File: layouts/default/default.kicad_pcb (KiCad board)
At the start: 2 copper layers, 27.1 x 34.7 mm, 18 parts

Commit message: fixed button
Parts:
- moved R3 0.10 mm to (77.1, 82.3)
- moved U3 0.07 mm to (73.2, 82.3)
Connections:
- net SUB2 renamed B8
- C1 pad 1: hv-1 -> hv
- C2 pad 1: hv -> hv-1
- C3 pad 1: hv -> hv-1
- C4 pad 1: hv -> hv-1
- C5 pad 1: hv -> hv-1
- C6 pad 1: hv -> hv-1
- C7 pad 1: hv -> hv-1
- R3 pad 1: hv -> hv-1
- U1 pad 2: hv -> hv-1
- U1 pad 3: hv-1 -> hv
- U1 pad 4: hv -> hv-1
- U2 pad 8: hv -> hv-1
- U4 pad 2: hv -> hv-1
- U5 pad A4: hv-1 -> hv
- U5 pad A9: hv-1 -> hv
- U5 pad B4: hv-1 -> hv
- U5 pad B9: hv-1 -> hv
- U6 pad 4: hv -> hv-1
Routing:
- net hv-1: track 27.3 -> 58.7 mm, vias 2 -> 4
- net hv: track 58.6 -> 27.3 mm, vias 4 -> 2

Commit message: updated button
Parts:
- removed R3: 10kΩ ±1% 62.5mW, atopile:R0402-56259e
- removed U3: , lib:KEY-SMD_4P-L4.2-W3.2-P2.20-LS4.6
- added R6: 10kΩ ±1% 62.5mW, atopile:R0402-56259e, F.Cu at (77.2, 82.2)
- added U7: , lib:KEY-SMD_4P-L4.2-W3.2-P2.20-LS4.6, F.Cu at (73.2, 82.2)
- C1, C2: value 10µF ±10% 25V X5R -> 100nF ±10% 50V X7R
- R1, R2: value 1kΩ ±1% 62.5mW -> 10kΩ ±1% 62.5mW
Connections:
- C1 pad 1: hv -> hv-1
- C2 pad 1: hv-1 -> hv
- C3 pad 1: hv-1 -> hv
- C4 pad 1: hv-1 -> hv
- C5 pad 1: hv-1 -> hv
- C6 pad 1: hv-1 -> hv
- C7 pad 1: hv-1 -> hv
- U1 pad 2: hv-1 -> hv
- U1 pad 3: hv -> hv-1
- U1 pad 4: hv-1 -> hv
- U2 pad 8: hv-1 -> hv
- U4 pad 2: hv-1 -> hv
- U4 pad 3: in -> EN
- U5 pad A4: hv -> hv-1
- U5 pad A9: hv -> hv-1
- U5 pad B4: hv -> hv-1
- U5 pad B9: hv -> hv-1
- U6 pad 4: hv-1 -> hv
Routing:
- net hv-1: track 58.7 -> 27.3 mm, vias 4 -> 2
- net hv: track 27.3 -> 58.7 mm, vias 2 -> 4
- net in: track 16.4 -> 18.7 mm

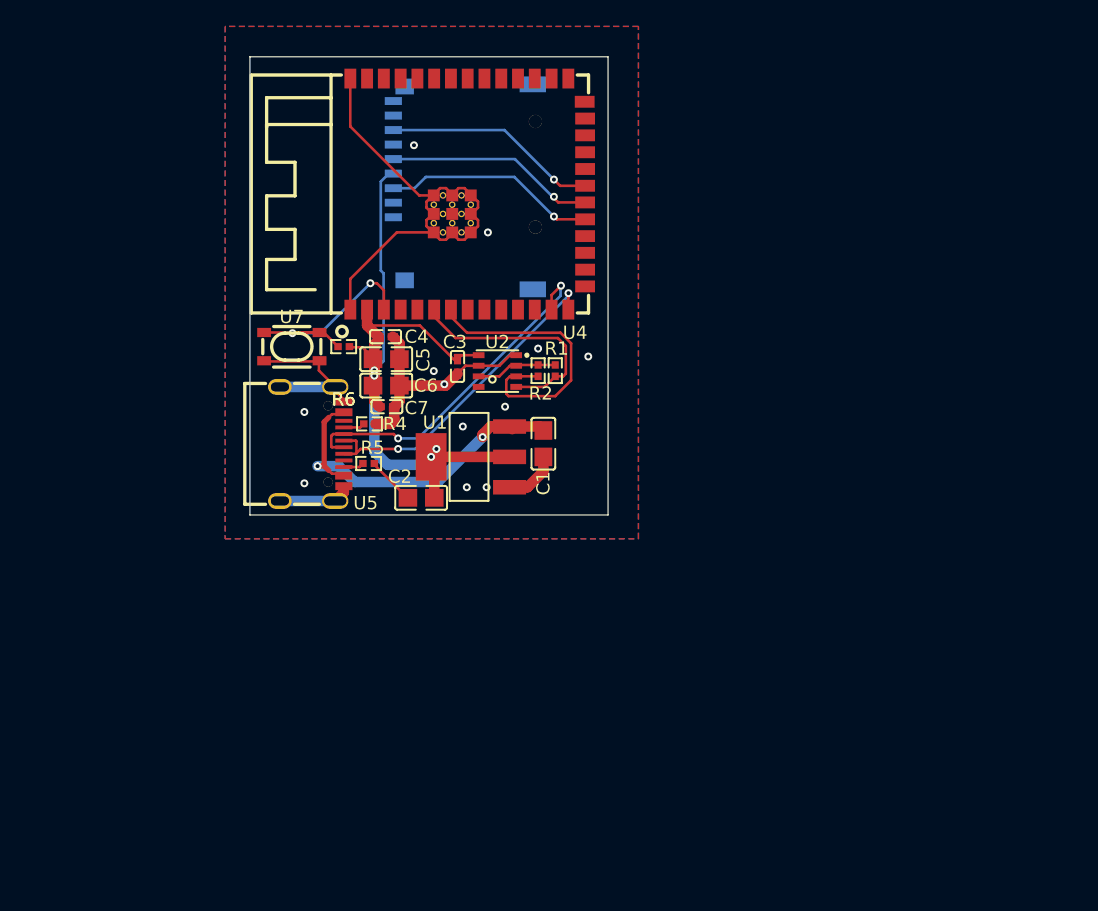
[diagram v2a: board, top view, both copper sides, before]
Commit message: added nose SPI interface, selectable number of sensors
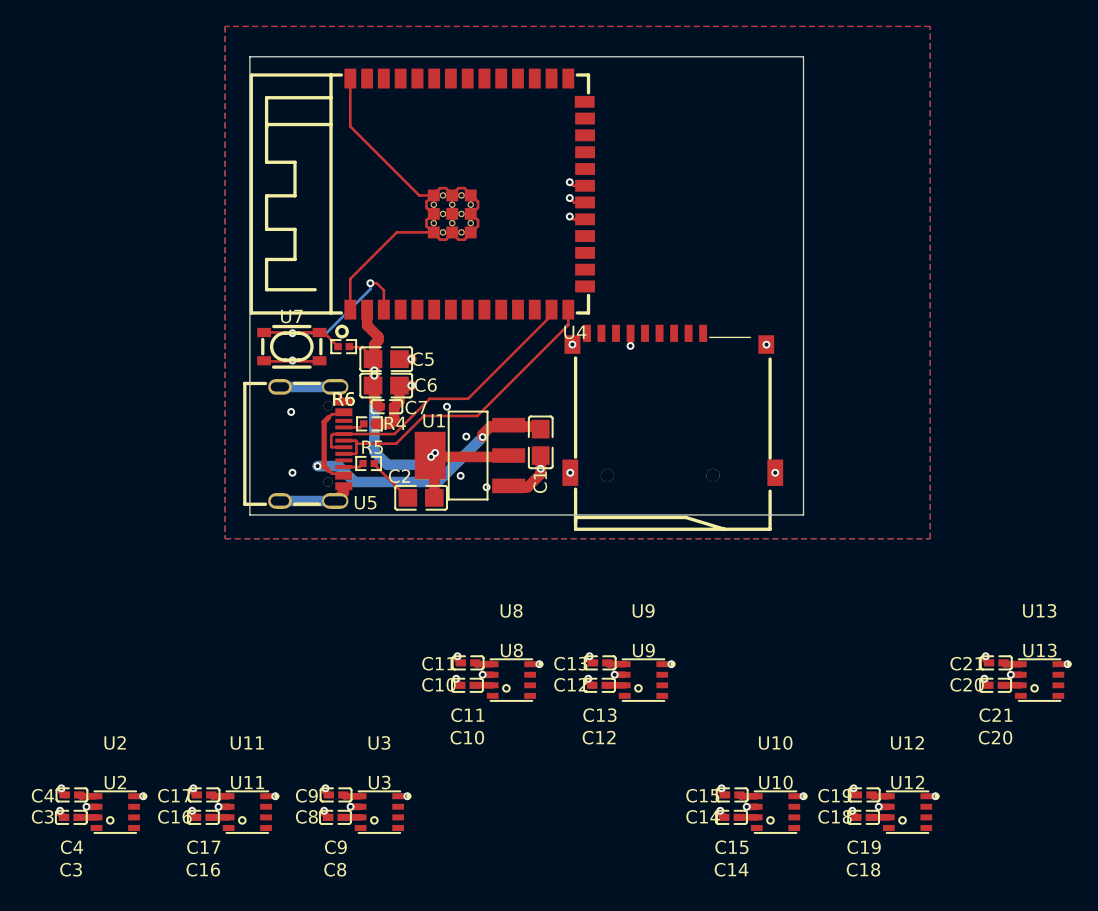
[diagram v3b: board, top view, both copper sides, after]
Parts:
- removed R1, R2: 10kΩ ±1% 62.5mW, atopile:R0402-56259e
- added C10: 100nF ±10% 16V X7R, atopile:C0402-b3ef17, F.Cu at (86.5, 107.9)
- added C11: 100nF ±10% 16V X7R, atopile:C0402-b3ef17, F.Cu at (86.6, 106.2)
- added C12: 100nF ±10% 16V X7R, atopile:C0402-b3ef17, F.Cu at (96.5, 107.9)
- added C13: 100nF ±10% 16V X7R, atopile:C0402-b3ef17, F.Cu at (96.6, 106.2)
- added C14: 100nF ±10% 16V X7R, atopile:C0402-b3ef17, F.Cu at (106.5, 117.9)
- added C15: 100nF ±10% 16V X7R, atopile:C0402-b3ef17, F.Cu at (106.6, 116.2)
- added C16: 100nF ±10% 16V X7R, atopile:C0402-b3ef17, F.Cu at (66.5, 117.9)
- added C17: 100nF ±10% 16V X7R, atopile:C0402-b3ef17, F.Cu at (66.6, 116.2)
- added C18: 100nF ±10% 16V X7R, atopile:C0402-b3ef17, F.Cu at (116.5, 117.9)
- added C19: 100nF ±10% 16V X7R, atopile:C0402-b3ef17, F.Cu at (116.6, 116.2)
- added C20: 100nF ±10% 16V X7R, atopile:C0402-b3ef17, F.Cu at (126.5, 107.9)
- added C21: 100nF ±10% 16V X7R, atopile:C0402-b3ef17, F.Cu at (126.6, 106.2)
- added C8: 100nF ±10% 16V X7R, atopile:C0402-b3ef17, F.Cu at (76.5, 117.9)
- added C9: 100nF ±10% 16V X7R, atopile:C0402-b3ef17, F.Cu at (76.6, 116.2)
- added U10: , atopile:LGA-8_L3.0-W3.0-P0.80_BME688-7465bb, F.Cu at (109.9, 117.5)
- added U11: , atopile:LGA-8_L3.0-W3.0-P0.80_BME688-7465bb, F.Cu at (69.9, 117.5)
- added U12: , atopile:LGA-8_L3.0-W3.0-P0.80_BME688-7465bb, F.Cu at (119.9, 117.5)
- added U13: , atopile:LGA-8_L3.0-W3.0-P0.80_BME688-7465bb, F.Cu at (129.9, 107.5)
- added U3: , atopile:LGA-8_L3.0-W3.0-P0.80_BME688-7465bb, F.Cu at (79.9, 117.5)
- added U8: , atopile:LGA-8_L3.0-W3.0-P0.80_BME688-7465bb, F.Cu at (89.9, 107.5)
- added U9: , atopile:LGA-8_L3.0-W3.0-P0.80_BME688-7465bb, F.Cu at (99.9, 107.5)
- C1, C2: value 100nF ±10% 50V X7R -> 10µF ±10% 25V X5R
- U6: moved to F.Cu
- moved C3 45.0 mm to (56.5, 117.9), turned to 180 degrees
- moved U2 44.2 mm to (59.9, 117.5)
- moved C4 42.0 mm to (56.6, 116.2), turned to 180 degrees
- moved U6 22.8 mm to (102.1, 86.5), turned to 0 degrees
- moved C1 0.22 mm to (92.1, 89.5)
- moved U1 0.12 mm to (86.7, 90.5)
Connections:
- net in renamed input
- C1 pad 1: hv-1 -> hv
- C2 pad 1: hv -> hv-1
- C3 pad 1: hv -> hv-1
- C4 pad 1: hv -> hv-1
- C5 pad 1: hv -> hv-1
- C6 pad 1: hv -> hv-1
- C7 pad 1: hv -> hv-1
- R6 pad 1: hv -> hv-1
- U1 pad 2: hv -> hv-1
- U1 pad 3: hv-1 -> hv
- U1 pad 4: hv -> hv-1
- U2 pad 2: CSB -> noses[0]-CSB
- U2 pad 6: CSB -> hv-1
- U2 pad 8: hv -> hv-1
- U4 pad : gnd -> (no net)
- U4 pad 19: CMD_DI_ -> SDI
- U4 pad 2: hv -> hv-1
- U4 pad 20: CLK_SCLK_ -> SCK
- U4 pad 21: DAT0_D0_ -> SDO
- U4 pad 6: SCK -> io6
- U4 pad 7: SDI -> io7
- U5 pad A4: hv-1 -> hv
- U5 pad A9: hv-1 -> hv
- U5 pad B4: hv-1 -> hv
- U5 pad B9: hv-1 -> hv
- U6 pad 3: CMD_DI_ -> SDI
- U6 pad 4: hv -> hv-1
- U6 pad 5: CLK_SCLK_ -> SCK
- U6 pad 7: DAT0_D0_ -> SDO
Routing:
- net hv: track 58.7 -> 27.1 mm, vias 4 -> 2
- net hv-1: track 27.3 -> 54.1 mm, vias 2 -> 4
- net SDI: track 22.3 -> 1.25 mm, vias 0 -> 1
- net DAT0_D0_: track 16.3 -> 0.00 mm, vias 1 -> 0
- net SCK: track 17.7 -> 1.44 mm, vias 0 -> 1
- net CMD_DI_: track 16.2 -> 0.00 mm, vias 1 -> 0
- net CLK_SCLK_: track 15.9 -> 0.00 mm, vias 1 -> 0
- net gnd: track 81.1 -> 88.9 mm, vias 12 -> 34
- net CSB: track 6.16 -> 0.00 mm
- net io19: track 26.7 -> 22.7 mm, vias 2 -> 0
- net io20: track 25.3 -> 23.9 mm, vias 2 -> 0
- net SDO: track 0.00 -> 1.27 mm, vias 0 -> 1
- net io6: track 0.00 -> 0.53 mm
- net (no net): vias 0 -> 13
- added copper zone on B.Cu, net (none)
- added copper zone on F.Cu, net (none)
- removed copper zone on B.Cu, net gnd
- removed copper zone on F.Cu, net gnd
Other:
- board size 27.1 x 34.7 mm -> 41.9 x 34.7 mm

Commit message: maintainence
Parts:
- C10, C11, C12, C13, C14, C15, C16, C17, C18, C19, C20, C21, C3, C4, C8, C9, U10, U11, U12, U13, U2, U3, U8, U9: moved to B.Cu
- moved U13 58.7 mm to (81.5, 74.3), turned to 90 degrees
- moved U2 56.5 mm to (81.5, 65.3), turned to 90 degrees
- moved C3 55.1 mm to (81.1, 68.6), turned to -90 degrees
- moved C20 54.6 mm to (81.1, 77.6), turned to -90 degrees
- moved C4 54.4 mm to (82.8, 68.5), turned to -90 degrees
- moved U12 53.0 mm to (89.0, 74.4), turned to 90 degrees
- moved U3 53.0 mm to (89.0, 65.3), turned to 90 degrees
- moved C21 52.3 mm to (82.8, 77.6), turned to -90 degrees
- moved U11 51.2 mm to (97.5, 74.4), turned to 90 degrees
- moved C8 50.7 mm to (88.6, 68.6), turned to -90 degrees
- moved C16 50.5 mm to (97.1, 77.7), turned to -90 degrees
- moved C17 50.2 mm to (98.8, 77.7), turned to -90 degrees
- moved C9 49.6 mm to (90.3, 68.6), turned to -90 degrees
- moved C18 48.9 mm to (88.6, 77.7), turned to -90 degrees
- moved C19 46.6 mm to (90.3, 77.7), turned to -90 degrees
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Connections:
- net A8 renamed SUB1
- net io10 renamed line
- C1 pad 1: hv -> hv-1
- C10 pad 1: hv-1 -> hv
- C11 pad 1: hv-1 -> hv
- C12 pad 1: hv-1 -> hv
- C13 pad 1: hv-1 -> hv
- C14 pad 1: hv-1 -> hv
- C15 pad 1: hv-1 -> hv
- C16 pad 1: hv-1 -> hv
- C17 pad 1: hv-1 -> hv
- C18 pad 1: hv-1 -> hv
- C19 pad 1: hv-1 -> hv
- C2 pad 1: hv-1 -> hv
- C20 pad 1: hv-1 -> hv
- C21 pad 1: hv-1 -> hv
- C3 pad 1: hv-1 -> hv
- C4 pad 1: hv-1 -> hv
- C5 pad 1: hv-1 -> hv
- C6 pad 1: hv-1 -> hv
- C7 pad 1: hv-1 -> hv
- C8 pad 1: hv-1 -> hv
- C9 pad 1: hv-1 -> hv
- R6 pad 1: hv-1 -> hv
- U1 pad 2: hv-1 -> hv
- U1 pad 3: hv -> hv-1
- U1 pad 4: hv-1 -> hv
- U10 pad 6: hv-1 -> hv
- U10 pad 8: hv-1 -> hv
- U11 pad 6: hv-1 -> hv
- U11 pad 8: hv-1 -> hv
- U12 pad 6: hv-1 -> hv
- U12 pad 8: hv-1 -> hv
- U13 pad 6: hv-1 -> hv
- U13 pad 8: hv-1 -> hv
- U2 pad 6: hv-1 -> hv
- U2 pad 8: hv-1 -> hv
- U3 pad 6: hv-1 -> hv
- U3 pad 8: hv-1 -> hv
- U4 pad 2: hv-1 -> hv
- U5 pad A4: hv -> hv-1
- U5 pad A9: hv -> hv-1
- U5 pad B4: hv -> hv-1
- U5 pad B9: hv -> hv-1
- U6 pad 4: hv-1 -> hv
- U8 pad 6: hv-1 -> hv
- U8 pad 8: hv-1 -> hv
- U9 pad 6: hv-1 -> hv
- U9 pad 8: hv-1 -> hv
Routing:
- net hv: track 27.1 -> 54.1 mm, vias 2 -> 4
- net hv-1: track 54.1 -> 27.1 mm, vias 4 -> 2

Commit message: doneish
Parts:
- R4, R5: value 4.7kΩ ±1% 62.5mW -> 5.1kΩ ±1% 62.5mW
- R6: value 10kΩ ±1% 62.5mW -> 10kΩ ±5% 62.5mW
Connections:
- net B8 renamed SUB2
- net SUB1 renamed A8
- U10 pad 2: noses[4]-CSB -> CSB-4
- U11 pad 2: noses[5]-CSB -> line
- U12 pad 2: noses[6]-CSB -> CSB-3
- U13 pad 2: noses[7]-CSB -> CSB-6
- U2 pad 2: noses[0]-CSB -> CSB-5
- U3 pad 2: noses[1]-CSB -> CSB-1
- U4 pad 16: io46 -> CSB-6
- U4 pad 17: io9 -> CSB-3
- U4 pad 22: io14 -> CSB-4
- U4 pad 23: io21 -> CSB
- U4 pad 24: io47 -> CSB-2
- U4 pad 25: io48 -> CSB-1
- U4 pad 26: io45 -> CSB-5
- U8 pad 2: noses[2]-CSB -> CSB-2
- U9 pad 2: noses[3]-CSB -> CSB
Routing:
- net SCK: track 1.44 -> 105.6 mm, vias 1 -> 2
- net SDO: track 1.27 -> 96.2 mm, vias 1 -> 3
- net SDI: track 1.25 -> 92.6 mm, vias 1 -> 2
- net hv: track 54.1 -> 135.2 mm, vias 4 -> 15
- net CSB-6: track 0.00 -> 15.5 mm, vias 0 -> 1
- net CSB-5: track 0.00 -> 14.1 mm, vias 0 -> 1
- net CSB-4: track 0.00 -> 13.5 mm, vias 0 -> 1
- net CSB: track 0.00 -> 12.6 mm, vias 0 -> 1
- net CSB-3: track 0.00 -> 6.69 mm, vias 0 -> 1
- net CSB-1: track 0.00 -> 6.63 mm, vias 0 -> 1
- net gnd: track 89.0 -> 93.6 mm, vias 34 -> 75
- net CSB-2: track 0.00 -> 3.94 mm, vias 0 -> 1
- net line: track 0.00 -> 2.74 mm, vias 0 -> 1
- net input: track 19.0 -> 17.8 mm
- net io20: track 23.6 -> 23.0 mm
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- added copper zone on B.Cu, net gnd
- added copper zone on F.Cu, net gnd
- removed copper zone on B.Cu, net (none)
- removed copper zone on F.Cu, net (none)

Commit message: meow
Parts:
- added C22: 100nF ±10% 16V X7R, atopile:C0402-b3ef17, F.Cu at (109.8, 65.0)
- added R1: 10kΩ ±1% 62.5mW, atopile:R0402-56259e, F.Cu at (105.1, 64.9)
- added R2: 10kΩ ±1% 62.5mW, atopile:R0402-56259e, F.Cu at (106.8, 74.2)
- added U14: , lib:LED-SMD_4P-L2.0-W2.0-BR, F.Cu at (109.7, 63.0)
- added U15: , lib:KEY-SMD_4P-L4.2-W3.2-P2.20-LS4.6, F.Cu at (103.7, 67.2)
- added U16: , lib:KEY-SMD_4P-L4.2-W3.2-P2.20-LS4.6, F.Cu at (103.7, 71.5)
- R6: value 10kΩ ±5% 62.5mW -> 10kΩ ±1% 62.5mW
- moved C6 0.41 mm to (80.8, 85.3)
- moved C5 0.40 mm to (80.8, 83.2)
- renumbered U4 to ESP32, U1 to LDO, U2 to SEN1, U3 to SEN2, U9 to SEN4, U13 to SEN5, U12 to SEN6, U11 to SEN7, U10 to SEN8
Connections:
- net A5 renamed CC1
- net A8 renamed SUB1
- net CC2 renamed B5
- net SUB2 renamed B8
- net input renamed input-1
- net io16 renamed line-2
- C1 pad 1: hv-1 -> hv
- C10 pad 1: hv -> hv-1
- C11 pad 1: hv -> hv-1
- C12 pad 1: hv -> hv-1
- C13 pad 1: hv -> hv-1
- C14 pad 1: hv -> hv-1
- C15 pad 1: hv -> hv-1
- C16 pad 1: hv -> hv-1
- C17 pad 1: hv -> hv-1
- C18 pad 1: hv -> hv-1
- C19 pad 1: hv -> hv-1
- C2 pad 1: hv -> hv-1
- C20 pad 1: hv -> hv-1
- C21 pad 1: hv -> hv-1
- C3 pad 1: hv -> hv-1
- C4 pad 1: hv -> hv-1
- C5 pad 1: hv -> hv-1
- C6 pad 1: hv -> hv-1
- C7 pad 1: hv -> hv-1
- C8 pad 1: hv -> hv-1
- C9 pad 1: hv -> hv-1
- ESP32 pad 16: CSB-6 -> CSB-3
- ESP32 pad 17: CSB-3 -> CSB-5
- ESP32 pad 18: line -> line-1
- ESP32 pad 2: hv -> hv-1
- ESP32 pad 23: CSB -> CSB-6
- ESP32 pad 24: CSB-2 -> CSB-1
- ESP32 pad 25: CSB-1 -> CSB
- ESP32 pad 26: CSB-5 -> CSB-2
- ESP32 pad 27: io0 -> DIN
- ESP32 pad 8: io15 -> line
- LDO pad 2: hv -> hv-1
- LDO pad 3: hv-1 -> hv
- LDO pad 4: hv -> hv-1
- R6 pad 1: hv -> hv-1
- SEN1 pad 2: CSB-5 -> CSB-2
- SEN1 pad 6: hv -> hv-1
- SEN1 pad 8: hv -> hv-1
- SEN2 pad 2: CSB-1 -> CSB
- SEN2 pad 6: hv -> hv-1
- SEN2 pad 8: hv -> hv-1
- SEN4 pad 2: CSB -> CSB-6
- SEN4 pad 6: hv -> hv-1
- SEN4 pad 8: hv -> hv-1
- SEN5 pad 2: CSB-6 -> CSB-3
- SEN5 pad 6: hv -> hv-1
- SEN5 pad 8: hv -> hv-1
- SEN6 pad 2: CSB-3 -> CSB-5
- SEN6 pad 6: hv -> hv-1
- SEN6 pad 8: hv -> hv-1
- SEN7 pad 2: line -> line-1
- SEN7 pad 6: hv -> hv-1
- SEN7 pad 8: hv -> hv-1
- SEN8 pad 6: hv -> hv-1
- SEN8 pad 8: hv -> hv-1
- U5 pad A4: hv-1 -> hv
- U5 pad A9: hv-1 -> hv
- U5 pad B4: hv-1 -> hv
- U5 pad B9: hv-1 -> hv
- U6 pad 4: hv -> hv-1
- U8 pad 2: CSB-2 -> CSB-1
- U8 pad 6: hv -> hv-1
- U8 pad 8: hv -> hv-1
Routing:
- net hv-1: track 27.0 -> 151.9 mm, vias 2 -> 9
- net hv: track 135.2 -> 26.8 mm, vias 15 -> 3
- net gnd: track 93.6 -> 158.0 mm, vias 75 -> 65
- net input-2: track 0.00 -> 20.9 mm, vias 0 -> 1
- net DIN: track 0.00 -> 15.9 mm
- net input: track 0.00 -> 11.9 mm, vias 0 -> 1
- net CSB-2: track 3.94 -> 14.3 mm
- net CSB-3: track 6.69 -> 15.7 mm
- net CSB-5: track 14.1 -> 6.96 mm
- net CSB: track 12.6 -> 6.83 mm
- net SDO: track 96.2 -> 100.3 mm
- net line: track 2.74 -> 0.00 mm, vias 1 -> 0
- net line-1: track 0.00 -> 2.64 mm, vias 0 -> 1
- net CSB-1: track 6.63 -> 4.06 mm
- net CSB-6: track 15.5 -> 13.0 mm
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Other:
- board size 41.9 x 34.7 mm -> 41.9 x 35.3 mm
- board text added: "RST"
- board text added: "START"
- board text added: "STATUS"
- board text added: "STOP"
- board text added: "lucy m 05/25"
- board text added: "meow"
- board text added: "non human scent"
- board text removed: "04/25/25 NonHumanScent"
- board text removed: "eigenlucy/nonhumanscent"

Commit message: fix designators and ready to order I think
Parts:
- renumbered LDO to U1, SEN8 to U10, SEN7 to U11, SEN6 to U12, SEN5 to U13, SEN1 to U2, SEN2 to U3, ESP32 to U4, SEN4 to U9
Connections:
- C1 pad 1: hv -> hv-1
- C10 pad 1: hv-1 -> hv
- C11 pad 1: hv-1 -> hv
- C12 pad 1: hv-1 -> hv
- C13 pad 1: hv-1 -> hv
- C14 pad 1: hv-1 -> hv
- C15 pad 1: hv-1 -> hv
- C16 pad 1: hv-1 -> hv
- C17 pad 1: hv-1 -> hv
- C18 pad 1: hv-1 -> hv
- C19 pad 1: hv-1 -> hv
- C2 pad 1: hv-1 -> hv
- C20 pad 1: hv-1 -> hv
- C21 pad 1: hv-1 -> hv
- C22 pad 1: hv-1 -> hv
- C3 pad 1: hv-1 -> hv
- C4 pad 1: hv-1 -> hv
- C5 pad 1: hv-1 -> hv
- C6 pad 1: hv-1 -> hv
- C7 pad 1: hv-1 -> hv
- C8 pad 1: hv-1 -> hv
- C9 pad 1: hv-1 -> hv
- R1 pad 1: hv-1 -> hv
- R2 pad 1: hv-1 -> hv
- R2 pad 2: input -> input-1
- R6 pad 1: hv-1 -> hv
- R6 pad 2: input-1 -> input
- U1 pad 2: hv-1 -> hv
- U1 pad 3: hv -> hv-1
- U1 pad 4: hv-1 -> hv
- U10 pad 6: hv-1 -> hv
- U10 pad 8: hv-1 -> hv
- U11 pad 2: line-1 -> line-2
- U11 pad 6: hv-1 -> hv
- U11 pad 8: hv-1 -> hv
- U12 pad 6: hv-1 -> hv
- U12 pad 8: hv-1 -> hv
- U13 pad 2: CSB-3 -> CSB
- U13 pad 6: hv-1 -> hv
- U13 pad 8: hv-1 -> hv
- U14 pad 1: hv-1 -> hv
- U16 pad 1: input -> input-1
- U16 pad 2: input -> input-1
- U2 pad 6: hv-1 -> hv
- U2 pad 8: hv-1 -> hv
- U3 pad 2: CSB -> CSB-1
- U3 pad 6: hv-1 -> hv
- U3 pad 8: hv-1 -> hv
- U4 pad 16: CSB-3 -> CSB
- U4 pad 18: line-1 -> line-2
- U4 pad 2: hv-1 -> hv
- U4 pad 24: CSB-1 -> CSB-3
- U4 pad 25: CSB -> CSB-1
- U4 pad 9: line-2 -> line-1
- U5 pad A4: hv -> hv-1
- U5 pad A9: hv -> hv-1
- U5 pad B4: hv -> hv-1
- U5 pad B9: hv -> hv-1
- U6 pad 4: hv-1 -> hv
- U7 pad 1: input-1 -> input
- U7 pad 2: input-1 -> input
- U8 pad 2: CSB-1 -> CSB-3
- U8 pad 6: hv-1 -> hv
- U8 pad 8: hv-1 -> hv
- U9 pad 6: hv-1 -> hv
- U9 pad 8: hv-1 -> hv
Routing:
- net hv-1: track 151.9 -> 26.8 mm, vias 9 -> 3
- net hv: track 26.8 -> 151.9 mm, vias 3 -> 9
- net input-2: track 20.9 -> 48.6 mm, vias 1 -> 2
- net input-1: track 17.9 -> 36.2 mm
- net CSB-3: track 15.7 -> 4.06 mm
- net CSB: track 6.83 -> 15.7 mm
- net input: track 11.9 -> 17.9 mm, vias 1 -> 2
- net CSB-1: track 4.06 -> 6.83 mm
- net line-2: track 0.00 -> 2.64 mm, vias 0 -> 1
- net line-1: track 2.64 -> 0.00 mm, vias 1 -> 0
- net gnd: track 158.0 -> 159.0 mm

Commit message: ordered
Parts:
- C1, C2: value 10µF ±10% 25V X5R -> 100nF ±10% 50V X7R
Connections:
- net SUB1 renamed A8
- R1 pad 2: input-2 -> input
- R6 pad 2: input -> input-2
- U10 pad 2: CSB-4 -> CSB-5
- U11 pad 2: line-2 -> line
- U12 pad 2: CSB-5 -> CSB
- U13 pad 2: CSB -> CSB-1
- U15 pad 1: input-2 -> input
- U15 pad 2: input-2 -> input
- U2 pad 2: CSB-2 -> CSB-4
- U3 pad 2: CSB-1 -> CSB-2
- U4 pad 16: CSB -> CSB-1
- U4 pad 17: CSB-5 -> CSB
- U4 pad 18: line-2 -> line
- U4 pad 22: CSB-4 -> CSB-5
- U4 pad 25: CSB-1 -> CSB-2
- U4 pad 26: CSB-2 -> CSB-4
- U4 pad 8: line -> line-1
- U4 pad 9: line-1 -> line-2
- U7 pad 1: input -> input-2
- U7 pad 2: input -> input-2
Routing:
- net input-2: track 48.6 -> 17.9 mm
- net input: track 17.9 -> 48.6 mm
- net CSB-1: track 6.83 -> 15.7 mm
- net CSB: track 15.7 -> 6.96 mm
- net CSB-2: track 14.3 -> 6.83 mm
- net CSB-5: track 6.96 -> 13.7 mm
- net line-2: track 2.64 -> 0.00 mm, vias 1 -> 0
- net line: track 0.00 -> 2.64 mm, vias 0 -> 1
- net CSB-4: track 13.7 -> 14.3 mm
